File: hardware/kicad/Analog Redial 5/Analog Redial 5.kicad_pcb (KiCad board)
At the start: 2 copper layers, 115 x 52 mm, 72 parts, among them J1 Barrel_Jack_PTH_Slot, J2 PINHD_1x8_Male, J3 PINHD_1x2_Male, J4 PINHD_1x2_Male, J5 PINHD_2x4_Male, J7 PINHD_1x3_Male, J8 RJ12, J9 RJ12, U1 ESP32-C6-DevKitC-1, U2 ES8388, U3 AG1171, U4 AG1171, U5 XC6206PxxxMR

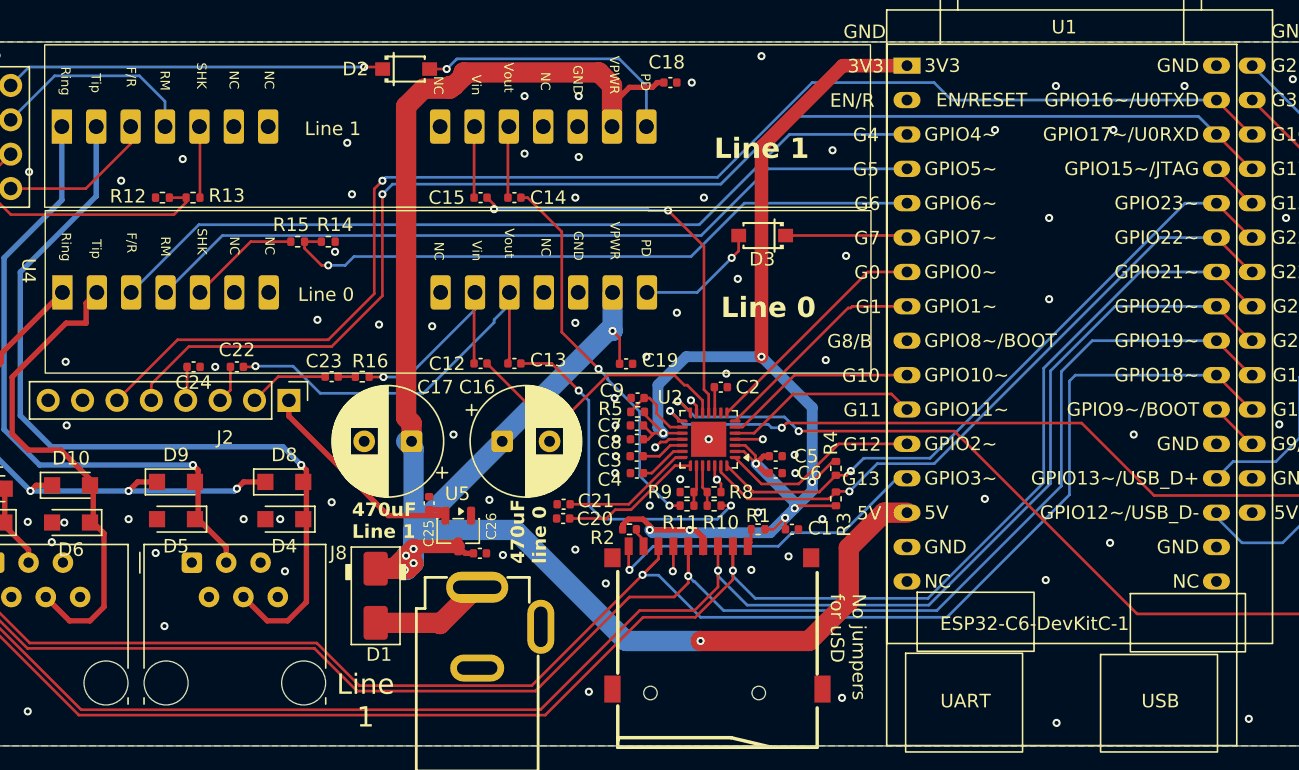
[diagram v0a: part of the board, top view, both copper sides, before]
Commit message: SMD5 + BM64 carrier: dedicated 3.3V rail, MFB pin, Vin protection, 8-pin link
Schematic work from the last few sessions' decisions:

SMD5 (Analog Redial 5)
- U5 XC6206P332MR (SOT-23) from +5V with C25/C26 1uF -> new +3V3_BM rail
  feeding the BM64 only, off the DevKit's own 3.3V
- BM64 header J12 -> J2, 6 -> 8 pins: +3V3_BM, AOHPL, MIC_P1, MIC_N1,
  U0RXD, U0TXD, MFB, GND
- MFB on GPIO15 with R17 100k pull-down (it's the BM64's power button --
  held from power-up it master-resets the pairing list)
- R16 1k in series into Line0Vin, and C23 10uF 0805 -> 1uF for the AOHPL
  coupling cap (Vin is 60k, not the few hundred ohms it was sized for)
- C24 1uF from MIC_N1 to GND (the differential mic input's AC ground)
- JP1 placed (Jumper_3_NC-1_Trace) for the planned MCLK/card-detect
  select, not wired yet

BM64 carrier board
- J2 -> J1, 8-pin socket mirroring the new SMD5 header, adding MIC_N1 and
  MFB
- New J2, 4-pin: P2_0 / RST_N / MFB, the one-time EEPROM-programming
  header that mates to J5 (replaces the loose J6/J10/J11 jumpers)

Co-Authored-By: Claude Opus 5 <noreply@anthropic.com>
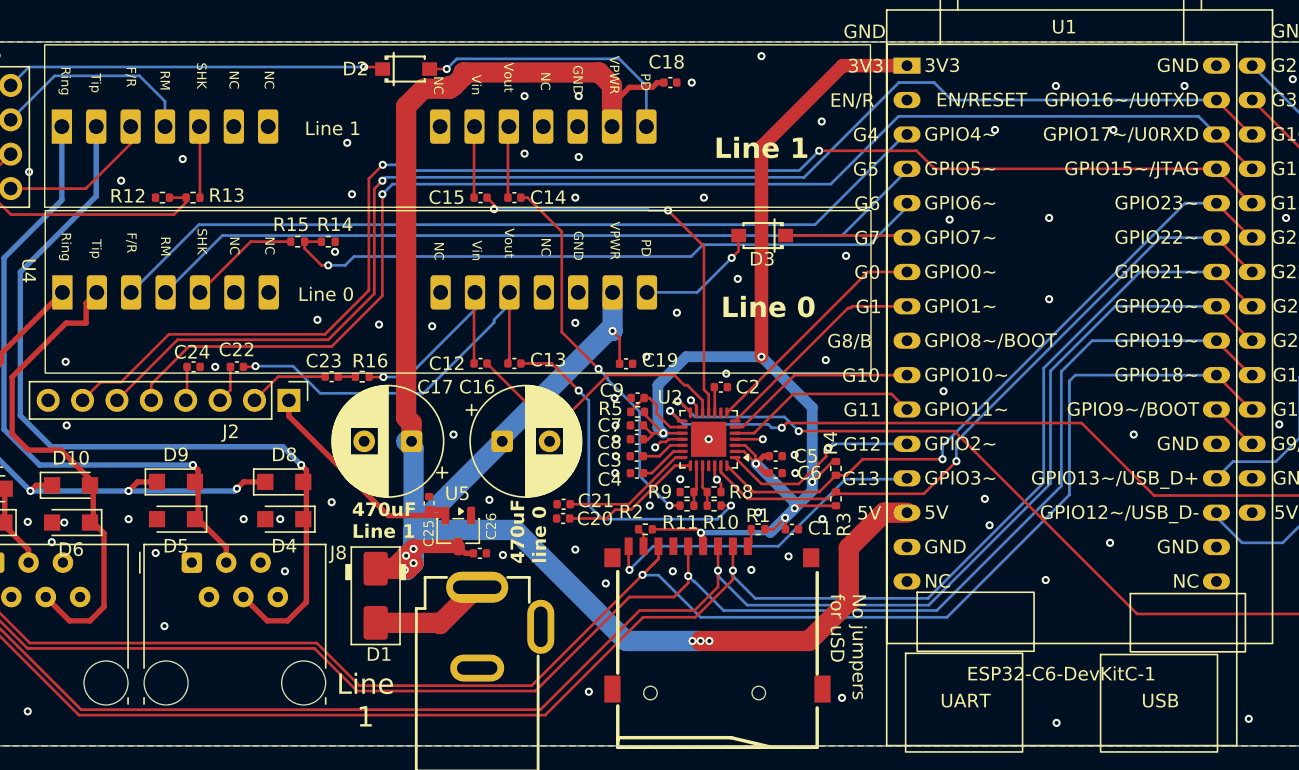
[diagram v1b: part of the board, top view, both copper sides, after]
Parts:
- moved R2 1.17 mm to (109.2, 86.0), turned to 180 degrees
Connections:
- J4 pad 1: /MFB -> Net-(U1-GPIO12/USB_D-)
- U1 pad 19: /MFB -> Net-(U1-GPIO12/USB_D-)
- U1 pad 29: unconnected-(U1-GPIO15/JTAG-Pad29) -> /MFB
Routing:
- net /MFB: track 46.3 -> 100.8 mm, vias 1 -> 2
- net Net-(U1-GPIO12/USB_D-): track 0.00 -> 46.3 mm, vias 0 -> 1
- net +3.3V: track 99.6 -> 92.6 mm, vias 8 -> 7
- net unconnected-(U1-GPIO15/JTAG-Pad29): track 3.69 -> 0.00 mm
- net GND: track 8.97 -> 7.74 mm, vias 86 -> 89
- net /SD_CLK: track 155.2 -> 154.2 mm
- net /I2C_SDA: track 49.6 -> 50.6 mm
- net /SD_CS: track 164.3 -> 163.7 mm
- net /I2C_SCL: track 49.5 -> 50.1 mm
- net /SD_MOSI: track 159.2 -> 159.8 mm
- net /SD_CD: track 24.5 -> 25.1 mm
- net /SD_MISO: track 151.3 -> 151.8 mm
- net /I2S_MCLK: track 14.7 -> 15.0 mm, vias 0 -> 1
- net +5V: vias 6 -> 8

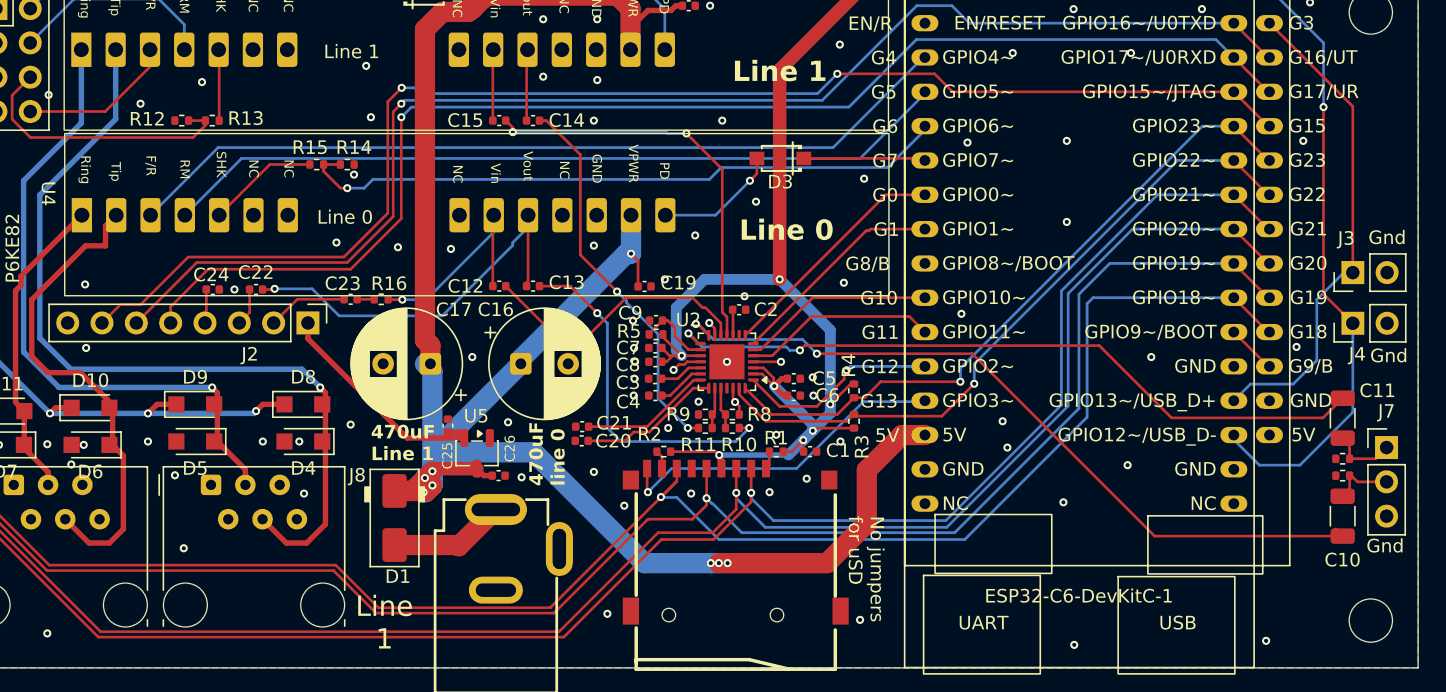
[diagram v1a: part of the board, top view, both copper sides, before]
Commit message: SMD5 + carrier: solder jumpers, C10/C11 to a disc footprint, 2-pin programming header
- SMD5: JP2/JP3 solder jumpers placed; C10/C11 100 uF 1206 -> 47 uF on
  Capacitor_THT:C_Disc_D4.7mm_W2.5mm_P5.00mm (DNP, fit 1 uF to use J7)
- Carrier: programming header down to 2 pins (P2_0, RST_N) now that MFB
  reaches the module through the main 8-pin link -- this also removes the
  hazard of MFB being driven from two connectors at once
- Cross-reference fixes missed by the hardware-doc split commit
- .gitignore: the Bluetooth carrier lives outside hardware/kicad/, so repeat
  the jlcpcb/, production_files/, tmp*.rpt and _restore_backup_* rules there

KNOWN ISSUE, not fixed here: carrier J1 pins 2 and 3 are swapped, so ESP TX
meets BM64 TX and ESP RX meets BM64 RX. See the next commit.

Co-Authored-By: Claude Opus 5 <noreply@anthropic.com>
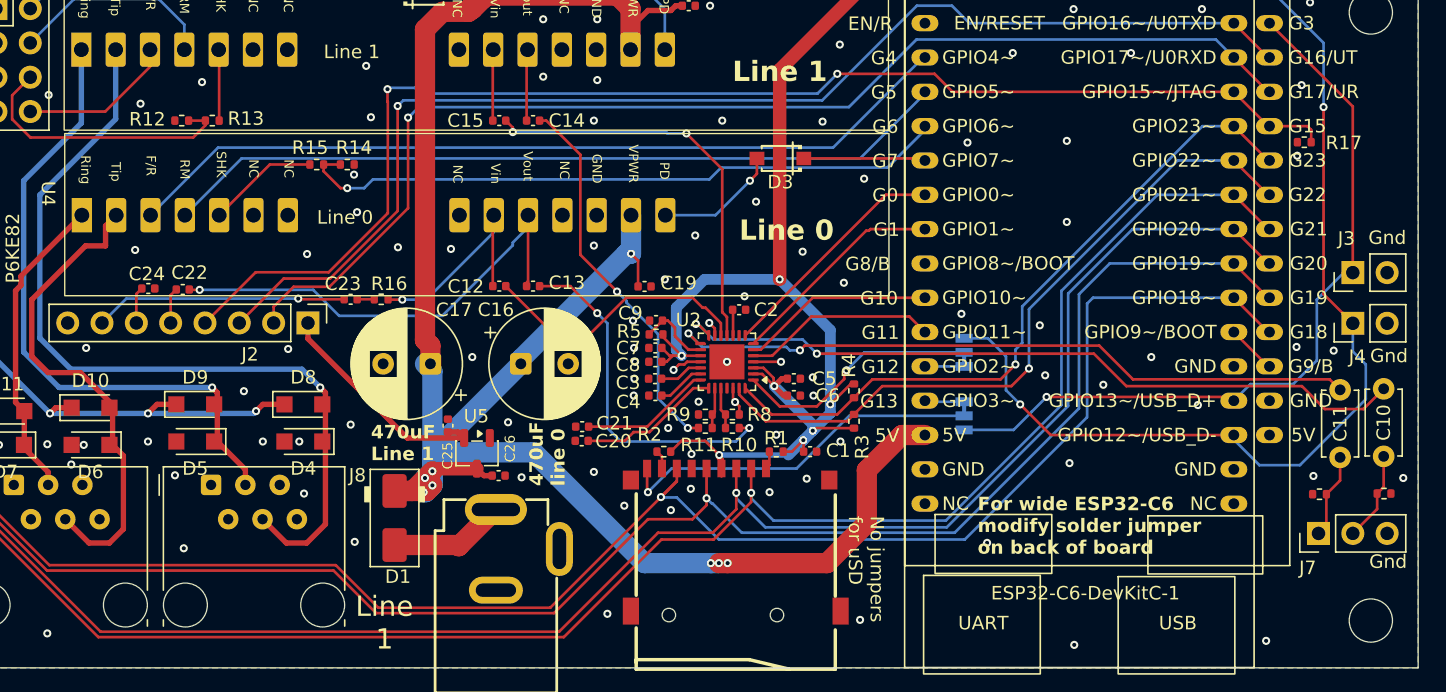
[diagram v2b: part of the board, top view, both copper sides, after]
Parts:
- added JP2: ~, PCM_SparkFun-Jumper:Jumper_3_NC-1_Trace_NoSilk, B.Cu at (131.4, 83.3)
- added JP3: ~, PCM_SparkFun-Jumper:Jumper_3_NC-1_Trace_NoSilk, B.Cu at (131.4, 78.7)
- added R17: 100k, Resistor_SMD:R_0402_1005Metric, F.Cu at (156.6, 63.1)
- added REF**: OSHW-Logo2_14.6x12mm_SilkScreen, Symbol:OSHW-Logo2_14.6x12mm_SilkScreen, B.Cu at (87.9, 60.7)
- C10, C11: value 100uF -> 47uF; footprint Capacitor_SMD:C_1206_3216Metric -> Capacitor_THT:C_Disc_D4.7mm_W2.5mm_P5.00mm
- moved J7 8.11 mm to (157.6, 92.0), turned to 90 degrees
- moved C22 5.42 mm to (73.6, 74.0)
- moved C10 5.37 mm to (162.4, 86.3), turned to 90 degrees
- moved C24 4.78 mm to (71.0, 73.9)
- moved R6 3.33 mm to (162.5, 89.1), turned to 180 degrees
- moved R7 3.14 mm to (157.7, 89.2)
- moved C11 2.91 mm to (159.2, 86.4)
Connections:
- net Net-(U1-GPIO12/USB_D-) renamed /GPIO12
- net Net-(U1-GPIO13/USB_D+) renamed /GPIO13
- J2 pad 2: Net-(C23-Pad2) -> Net-(U1-GPIO17/U0RXD)
- J2 pad 3: Net-(C22-Pad2) -> Net-(U1-GPIO16/U0TXD)
- J2 pad 4: Net-(C24-Pad2) -> /MFB
- J2 pad 5: Net-(U1-GPIO17/U0RXD) -> Net-(C22-Pad2)
- J2 pad 6: Net-(U1-GPIO16/U0TXD) -> Net-(C24-Pad2)
- J2 pad 7: /MFB -> Net-(C23-Pad2)
- U1 pad 12: /I2S_MCLK -> Net-(JP3-A)
- U1 pad 13: /SD_CD -> Net-(JP2-A)
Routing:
- net /GPIO12: track 46.3 -> 71.5 mm, vias 1 -> 2
- net /GPIO13: track 36.4 -> 57.5 mm, vias 0 -> 1
- net Net-(C23-Pad2): track 5.94 -> 18.7 mm, vias 0 -> 1
- net Net-(U1-GPIO17/U0RXD): track 96.3 -> 88.2 mm
- net Net-(U1-GPIO16/U0TXD): track 99.7 -> 92.1 mm
- net /Line0Vout: track 29.3 -> 34.7 mm
- net /I2S_MCLK: track 15.0 -> 18.3 mm
- net Net-(JP2-A): track 0.00 -> 3.03 mm
- net /MFB: track 100.8 -> 97.9 mm
- net Net-(JP3-A): track 0.00 -> 2.91 mm
- net /SD_CD: track 25.1 -> 27.5 mm
- net Net-(U2-LOUT2): track 53.5 -> 51.5 mm
- net Net-(C10-Pad1): track 4.76 -> 6.70 mm
- net Net-(C11-Pad1): track 5.41 -> 7.08 mm
- net /I2C_SCL: track 50.1 -> 51.7 mm
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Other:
- board text added: "Analog Redial 5"
- board text added: "For wide ESP32-C6 modify solder jumper on back of board"
- board text added: "For wide esp32-c6 cut jumpers bridge pads"
- board text added: "GPIO12"
- board text added: "GPIO13"
- board text removed: "GPIO12~/USB_D-"
- board text removed: "GPIO13~/USB_D+"
- board text removed: "GPIO2~"
- board text removed: "GPIO3~"

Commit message: kicad: consolidate custom footprints/3D/symbols into libraries/
Move all per-project Scott.pretty, JLCImport.pretty, .3dshapes, and
.kicad_sym files into a single shared kicad/libraries/ directory.
Rename "Scott" library to "Custom" throughout. Update fp-lib-table,
sym-lib-table, .kicad_pcb, and .kicad_sch files in all 6 board
projects to resolve Custom: and JLCImport: via ${KIPRJMOD}/../libraries/.

Also fixes broken 3D model paths (hardcoded /Users/... and
_restore_backup_ references in SMD3/SMD4/AR5 PCBs).

Generated with [Devin](https://devin.ai)

Co-Authored-By: Devin <158243242+devin-ai-integration[bot]@users.noreply.github.com>
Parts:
- J8, J9: footprint Scott:RJ12_Amphenol_87180_Horizontal -> Custom:RJ12_Amphenol_87180_Horizontal
- U1: footprint Scott:ESP32-C6-DevKitC-dual -> Custom:ESP32-C6-DevKitC-dual
- U3, U4: footprint Scott:AG1171_SIL -> Custom:AG1171_SIL
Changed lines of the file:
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@@
 		)
 	)
-	(footprint "Scott:AG1171_SIL"
+	(footprint "Custom:AG1171_SIL"
 		(locked yes)
 		(layer "F.Cu")
@@
 		)
 		(embedded_fonts no)
-		(model "/Users/sdylewski/Documents/Projects/esp32_rotary_phone/hardware/kicad/Rotary_phone_SMD4/Scott.3dshapes/AG1171.step"
+		(model "${KIPRJMOD}/../libraries/Custom.3dshapes/AG1171.step"
 			(offset
 				(xyz 31.25 4.3 0)
@@
 		)
 	)
-	(footprint "Scott:ESP32-C6-DevKitC-dual"
+	(footprint "Custom:ESP32-C6-DevKitC-dual"
 		(layer "F.Cu")
 		(at 128.5 51.75)
@@
 		)
 		(embedded_fonts no)
-		(model "/Users/sdylewski/Documents/Projects/esp32_rotary_phone/hardware/kicad/Rotary_phone_SMD4/JLCImport.3dshapes/TF-01A.step"
+		(model "${KIPRJMOD}/../libraries/JLCImport.3dshapes/TF-01A.step"
 			(offset
 				(xyz 0.002223 -5.10134 0.14732)
@@
 		)
 	)
-	(footprint "Scott:RJ12_Amphenol_87180_Horizontal"
+	(footprint "Custom:RJ12_Amphenol_87180_Horizontal"
 		(layer "F.Cu")
 		(at 61.07 88.46)
@@
 		)
 		(embedded_fonts no)
-		(model "/Users/sdylewski/Documents/Projects/esp32_rotary_phone/hardware/kicad/Rotary_phone_SMD4/Scott.3dshapes/87180-062LF.step"
+		(model "${KIPRJMOD}/../libraries/Custom.3dshapes/87180-062LF.step"
 			(offset
 				(xyz 3.2 -8.78 0)
@@
 		)
 		(embedded_fonts no)
-		(model "${KIPRJMOD}/_restore_backup_2026-08-30T20-24-25-026/JLCImport.3dshapes/1N4148W_C81598.step"
+		(model "${KIPRJMOD}/../libraries/JLCImport.3dshapes/1N4148W_C81598.step"
 			(offset
 				(xyz 0 0 0)
@@
 		)
 	)
-	(footprint "Scott:AG1171_SIL"
+	(footprint "Custom:AG1171_SIL"
 		(locked yes)
 		(layer "F.Cu")
@@
 		)
 		(embedded_fonts no)
-		(model "/Users/sdylewski/Documents/Projects/esp32_rotary_phone/hardware/kicad/Rotary_phone_SMD4/Scott.3dshapes/AG1171.step"
+		(model "${KIPRJMOD}/../libraries/Custom.3dshapes/AG1171.step"
 			(offset
 				(xyz 31.25 4.3 0)
@@
 		)
 	)
-	(footprint "Scott:RJ12_Amphenol_87180_Horizontal"
+	(footprint "Custom:RJ12_Amphenol_87180_Horizontal"
 		(layer "F.Cu")
 		(at 75.67 88.46)
@@
 		)
 		(embedded_fonts no)
-		(model "/Users/sdylewski/Documents/Projects/esp32_rotary_phone/hardware/kicad/Rotary_phone_SMD4/Scott.3dshapes/87180-062LF.step"
+		(model "${KIPRJMOD}/../libraries/Custom.3dshapes/87180-062LF.step"
 			(offset
 				(xyz 3.2 -8.78 0)
@@
 		)
 		(embedded_fonts no)
-		(model "${KIPRJMOD}/_restore_backup_2026-08-30T20-24-25-026/JLCImport.3dshapes/1N4148W_C81598.step"
+		(model "${KIPRJMOD}/../libraries/JLCImport.3dshapes/1N4148W_C81598.step"
 			(offset
 				(xyz 0 0 0)
